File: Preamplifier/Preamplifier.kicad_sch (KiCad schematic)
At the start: 0 parts

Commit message: Preamplifier Schematic
Added the preamplifier schematic.
Updated the preamplifier project.
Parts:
- added C1, C10, C13, C14, C2, C23, C24, C5, C6, C9: 100n, Capacitor_SMD:C_0805_2012Metric_Pad1.18x1.45mm_HandSolder, symbol Device:C
- added C11, C12: 22n, Capacitor_SMD:C_0805_2012Metric_Pad1.18x1.45mm_HandSolder, symbol Device:C
- added C15, C16, C17, C18, C19, C20, C25, C26: 1u, Capacitor_SMD:C_0805_2012Metric_Pad1.18x1.45mm_HandSolder, symbol Device:C
- added C21, C22, C7, C8: 22u, Capacitor_SMD:CP_Elec_6.3x5.8, symbol Device:C_Polarized
- added C3, C4: 100p, Capacitor_SMD:C_0805_2012Metric_Pad1.18x1.45mm_HandSolder, symbol Device:C
- added H1, H2, H3, H4: MountingHole, MountingHole:MountingHole_3.2mm_M3, symbol Mechanical:MountingHole
- added J1: POWER, Connector_Molex:Molex_KK-254_AE-6410-03A_1x03_P2.54mm_Vertical, symbol Connector:Conn_01x03_Pin
- added J2: IN_L, Connector_Molex:Molex_KK-254_AE-6410-02A_1x02_P2.54mm_Vertical, symbol Connector_Generic:Conn_01x02
- added J3: IN_R, Connector_Molex:Molex_KK-254_AE-6410-02A_1x02_P2.54mm_Vertical, symbol Connector_Generic:Conn_01x02
- added J4: OUT_L, Connector_Molex:Molex_KK-254_AE-6410-02A_1x02_P2.54mm_Vertical, symbol Connector_Generic:Conn_01x02
- added J5: OUT_R, Connector_Molex:Molex_KK-254_AE-6410-02A_1x02_P2.54mm_Vertical, symbol Connector_Generic:Conn_01x02
- added R1, R11, R12, R2: 47K, Resistor_SMD:R_0805_2012Metric_Pad1.20x1.40mm_HandSolder, symbol Device:R
- added R10, R9: 10K, Resistor_SMD:R_0805_2012Metric_Pad1.20x1.40mm_HandSolder, symbol Device:R
- added R13, R14: 90K9, Resistor_SMD:R_0805_2012Metric_Pad1.20x1.40mm_HandSolder, symbol Device:R
- added R15, R16: 6K36, Resistor_SMD:R_0805_2012Metric_Pad1.20x1.40mm_HandSolder, symbol Device:R
- added R17, R18: 2K7, Resistor_SMD:R_0805_2012Metric_Pad1.20x1.40mm_HandSolder, symbol Device:R
- added R19, R20, R23, R24: 100K, Resistor_SMD:R_0805_2012Metric_Pad1.20x1.40mm_HandSolder, symbol Device:R
- added R21, R22: 750, Resistor_SMD:R_0805_2012Metric_Pad1.20x1.40mm_HandSolder, symbol Device:R
- added R3, R4: 2K2, Resistor_SMD:R_0805_2012Metric_Pad1.20x1.40mm_HandSolder, symbol Device:R
- added R5, R6: 4K7, Resistor_SMD:R_0805_2012Metric_Pad1.20x1.40mm_HandSolder, symbol Device:R
- added R7, R8: 180K, Resistor_SMD:R_0805_2012Metric_Pad1.20x1.40mm_HandSolder, symbol Device:R
- added U1, U2, U3, U4: OPA1612AxD, Package_SO:SOIC-8_3.9x4.9mm_P1.27mm, symbol Amplifier_Operational:OPA1612AxD
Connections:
- new net: C16.1, R10.2, R8.2, U3.1
- new net: C16.2, C18.1, R12.2
- new net: C2.1, U1.4 (V-)
- new net: C6.1, U2.4 (V-)
- new net: C5.2, U2.8 (V+)
- new net: C15.1, R7.2, R9.2, U1.1
- new net: C15.2, C17.1, R11.2
- new net: U1.6 (-), U1.7
- new net: C19.1, R11.1, U2.1, U2.2 (-)
- new net: C19.2, R15.1, U2.5 (+)
- new net: C26.2, J5.2 (Pin_2), R24.1
- new net: R17.1, R19.1, U2.6 (-)
- new net: R19.2, R21.1, U2.7
- new net: C25.2, J4.2 (Pin_2), R23.1
- new net: C23.1, C25.1, R21.2
- new net: C20.1, R12.1, U4.1, U4.2 (-)
- new net: C20.2, R16.1, U4.5 (+)
- new net: C4.1, J3.2 (Pin_2), R2.1, R4.1
- new net: R4.2, U3.3 (+)
- new net: C13.2, U4.8 (V+)
- new net: C3.1, J2.2 (Pin_2), R1.1, R3.1
- new net: C17.2, R13.1, U2.3 (+)
- new net: C11.1, R5.1, R7.1, U1.2 (-)
- new net: C7.1, R5.2
- new net: C1.2, U1.8 (V+)
- new net: C18.2, R14.1, U4.3 (+)
- new net: C14.1, U4.4 (V-)
- new net: R18.1, R20.1, U4.6 (-)
- new net: C22.1, R18.2
- new net: C12.1, R6.1, R8.1, U3.2 (-)
- new net: C12.2, R10.1
- new net: C24.1, C26.1, R22.2
- new net: C21.1, R17.2
- new net: C8.1, R6.2
- new net: C10.1, U3.4 (V-)
- new net: C9.2, U3.8 (V+)
- new net: R20.2, R22.1, U4.7
- new net: U3.6 (-), U3.7
- new net: C11.2, R9.1
- new net: R3.2, U1.3 (+)
- new net +12V: C1.1, C13.1, C5.1, C9.1, J1.1 (Pin_1)
- new net -12V: C10.2, C14.2, C2.2, C6.2, J1.3 (Pin_3)
- new net GND: C21.2, C22.2, C23.2, C24.2, C3.2, C4.2, C7.2, C8.2, J1.2 (Pin_2), J2.1 (Pin_1), J3.1 (Pin_1), J4.1 (Pin_1), J5.1 (Pin_1), R1.2, R13.2, R14.2, R15.2, R16.2, R2.2, R23.2, R24.2, U1.5 (+), U3.5 (+)

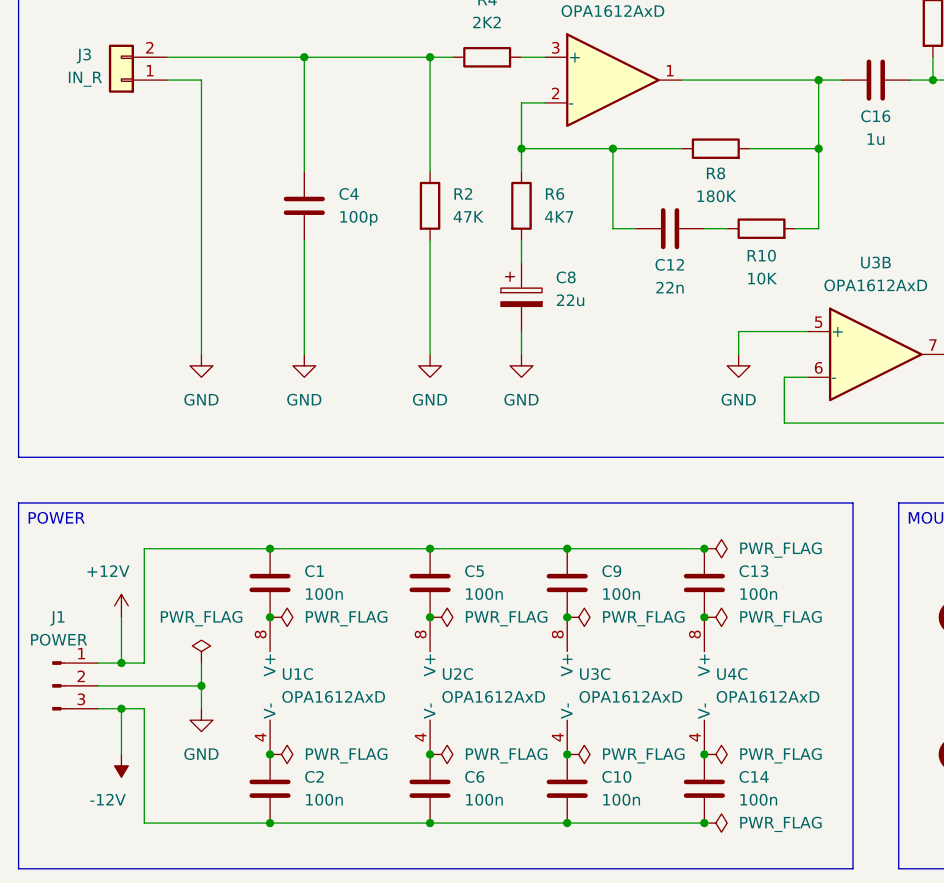
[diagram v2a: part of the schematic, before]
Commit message: Preamplifier Board
Updated the preamplifier board design.
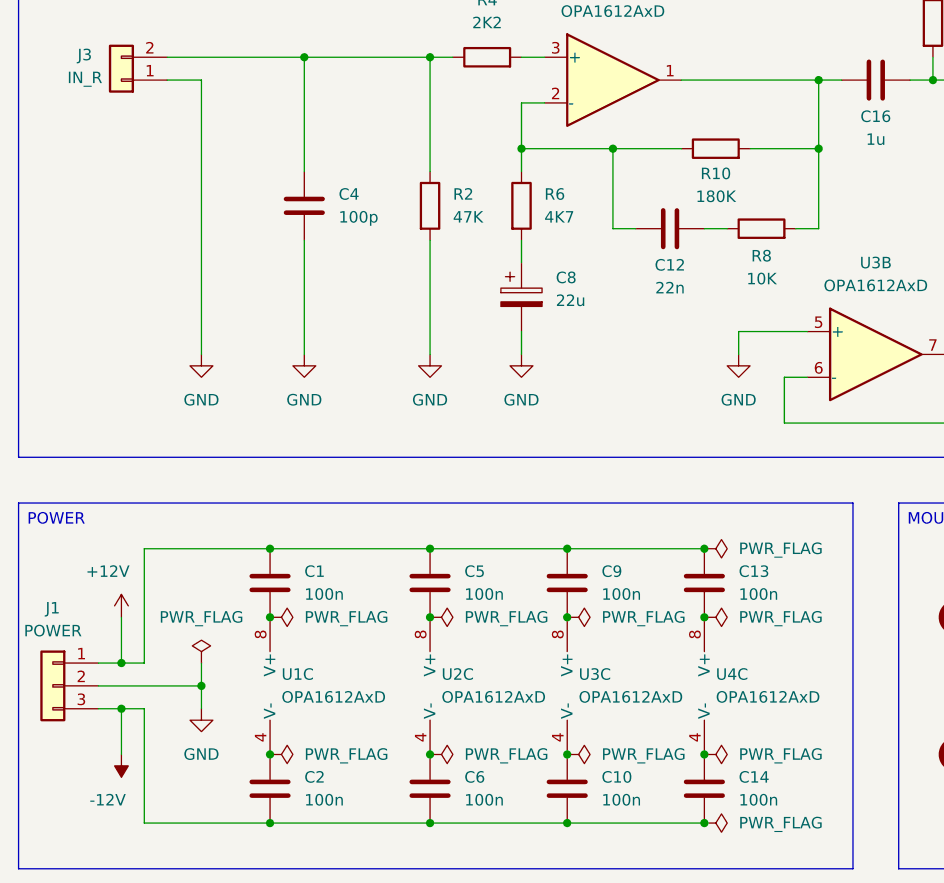
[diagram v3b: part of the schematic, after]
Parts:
- removed J1: POWER, Connector_Molex:Molex_KK-254_AE-6410-03A_1x03_P2.54mm_Vertical, symbol Connector:Conn_01x03_Pin
- added J1: POWER, Custom_Parts:Molex_KK-254_1x03_P2.54mm_Vertical, symbol Connector_Generic:Conn_01x03
- J2, J3, J4, J5: footprint Connector_Molex:Molex_KK-254_AE-6410-02A_1x02_P2.54mm_Vertical -> Custom_Parts:Molex_KK-254_1x02_P2.54mm_Vertical
- renumbered R8 to R10, R10 to R8
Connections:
- net +12V: now also J1.1 (Pin_1)
- net -12V: now also J1.3 (Pin_3)
- net GND: now also J1.2 (Pin_2)
- net at J5.2 (Pin_2), R24.1: now also C26.1; no longer C26.2
- net at C24.1, R22.2: now also C26.2; no longer C26.1
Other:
- moved on the sheet: C26
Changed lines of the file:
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@@
 			)
 		)
-		(property "Footprint" "Connector_Molex:Molex_KK-254_AE-6410-02A_1x02_P2.54mm_Vertical"
+		(property "Footprint" "Custom_Parts:Molex_KK-254_1x02_P2.54mm_Vertical"
 			(at 254 107.95 0)
 			(effects
@@
 	)
 	(symbol
-		(lib_id "Connector:Conn_01x03_Pin")
-		(at 30.48 172.72 0)
-		(unit 1)
-		(exclude_from_sim no)
-		(in_bom yes)
-		(on_board yes)
-		(dnp no)
-		(fields_autoplaced yes)
-		(property "Reference" "J1"
-			(at 31.115 165.1 0)
-			(effects
-				(font
-					(size 1.27 1.27)
-				)
-			)
-		)
-		(property "Value" "POWER"
-			(at 31.115 167.64 0)
-			(effects
-				(font
-					(size 1.27 1.27)
-				)
-			)
-		)
-		(property "Footprint" "Connector_Molex:Molex_KK-254_AE-6410-03A_1x03_P2.54mm_Vertical"
-			(at 30.48 172.72 0)
-			(effects
-				(font
-					(size 1.27 1.27)
-				)
-				(hide yes)
-			)
-		)
-		(property "Datasheet" "~"
-			(at 30.48 172.72 0)
-			(effects
-				(font
-					(size 1.27 1.27)
-				)
-				(hide yes)
-			)
-		)
-		(property "Description" "Generic connector, single row, 01x03, script generated"
-			(at 30.48 172.72 0)
-			(effects
-				(font
-					(size 1.27 1.27)
-				)
-				(hide yes)
-			)
-		)
-		(pin "1"
-		)
-		(pin "3"
-		)
-		(pin "2"
-		)
-		(instances
-			(project ""
-				(path "/506a4015-8700-461c-aa21-0f1930354b08"
-					(reference "J1")
-					(unit 1)
-				)
-			)
-		)
-	)
-	(symbol
 		(lib_id "power:GND")
 		(at 220.98 69.85 0)
@@
 		(dnp no)
 		(fields_autoplaced yes)
-		(property "Reference" "#FLG09"
+		(property "Reference" "#FLG010"
 			(at 104.775 180.34 0)
 			(effects
@@
 			(project "Preamplifier"
 				(path "/506a4015-8700-461c-aa21-0f1930354b08"
-					(reference "#FLG09")
+					(reference "#FLG010")
 					(unit 1)
 				)
@@
 			)
 		)
-		(property "Footprint" "Connector_Molex:Molex_KK-254_AE-6410-02A_1x02_P2.54mm_Vertical"
+		(property "Footprint" "Custom_Parts:Molex_KK-254_1x02_P2.54mm_Vertical"
 			(at 38.1 39.37 0)
 			(effects
@@
 			)
 		)
-		(property "Footprint" "Connector_Molex:Molex_KK-254_AE-6410-02A_1x02_P2.54mm_Vertical"
+		(property "Footprint" "Custom_Parts:Molex_KK-254_1x02_P2.54mm_Vertical"
 			(at 254 41.91 0)
 			(effects
@@
 	(symbol
 		(lib_id "Device:C")
-		(at 227.33 105.41 90)
+		(at 227.33 105.41 270)
+		(mirror x)
 		(unit 1)
 		(exclude_from_sim no)
@@
 		(on_board yes)
 		(dnp no)
-		(fields_autoplaced yes)
 		(property "Reference" "C26"
 			(at 227.33 97.79 90)
@@
 		)
 		(property "Footprint" "Capacitor_SMD:C_0805_2012Metric_Pad1.18x1.45mm_HandSolder"
-			(at 231.14 104.4448 0)
+			(at 223.52 104.4448 0)
 			(effects
 				(font
@@
 			)
 		)
-		(property "Footprint" "Connector_Molex:Molex_KK-254_AE-6410-02A_1x02_P2.54mm_Vertical"
+		(property "Footprint" "Custom_Parts:Molex_KK-254_1x02_P2.54mm_Vertical"
 			(at 38.1 105.41 0)
 			(effects
@@
 		(on_board yes)
 		(dnp no)
-		(property "Reference" "R10"
+		(property "Reference" "R8"
 			(at 109.22 124.968 90)
 			(effects
@@
 			(project "Preamplifier"
 				(path "/506a4015-8700-461c-aa21-0f1930354b08"
-					(reference "R10")
+					(reference "R8")
 					(unit 1)
 				)
@@
 		(dnp no)
 		(fields_autoplaced yes)
-		(property "Reference" "#FLG08"
+		(property "Reference" "#FLG09"
 			(at 104.775 165.1 0)
 			(effects
@@
 			(project "Preamplifier"
 				(path "/506a4015-8700-461c-aa21-0f1930354b08"
-					(reference "#FLG08")
+					(reference "#FLG09")
 					(unit 1)
 				)
@@
 		(on_board yes)
 		(dnp no)
-		(property "Reference" "R8"
+		(property "Reference" "R10"
 			(at 104.14 115.824 90)
 			(effects
@@
 			(project "Preamplifier"
 				(path "/506a4015-8700-461c-aa21-0f1930354b08"
-					(reference "R8")
+					(reference "R10")
 					(unit 1)
 				)
@@
 	)
 	(symbol
+		(lib_id "Connector_Generic:Conn_01x03")
+		(at 30.48 172.72 0)
+		(mirror y)
+		(unit 1)
+		(exclude_from_sim no)
+		(in_bom yes)
+		(on_board yes)
+		(dnp no)
+		(property "Reference" "J1"
+			(at 30.48 164.084 0)
+			(effects
+				(font
+					(size 1.27 1.27)
+				)
+			)
+		)
+		(property "Value" "POWER"
+			(at 30.48 166.624 0)
+			(effects
+				(font
+					(size 1.27 1.27)
+				)
+			)
+		)
+		(property "Footprint" "Custom_Parts:Molex_KK-254_1x03_P2.54mm_Vertical"
+			(at 30.48 172.72 0)
+			(effects
+				(font
+					(size 1.27 1.27)
+				)
+				(hide yes)
+			)
+		)
+		(property "Datasheet" "~"
+			(at 30.48 172.72 0)
+			(effects
+				(font
+					(size 1.27 1.27)
+				)
+				(hide yes)
+			)
+		)
+		(property "Description" "Generic connector, single row, 01x03, script generated (kicad-library-utils/schlib/autogen/connector/)"
+			(at 30.48 172.72 0)
+			(effects
+				(font
+					(size 1.27 1.27)
+				)
+				(hide yes)
+			)
+		)
+		(pin "1"
+		)
+		(pin "2"
+		)
+		(pin "3"
+		)
+		(instances
+			(project ""
+				(path "/506a4015-8700-461c-aa21-0f1930354b08"
+					(reference "J1")
+					(unit 1)
+				)
+			)
+		)
+	)
+	(symbol
 		(lib_id "Device:R")
 		(at 185.42 53.34 0)
@@
 		(dnp no)
 		(fields_autoplaced yes)
-		(property "Reference" "#FLG010"
+		(property "Reference" "#FLG08"
 			(at 104.775 157.48 0)
 			(effects
@@
 			(project "Preamplifier"
 				(path "/506a4015-8700-461c-aa21-0f1930354b08"
-					(reference "#FLG010")
+					(reference "#FLG08")
 					(unit 1)
 				)

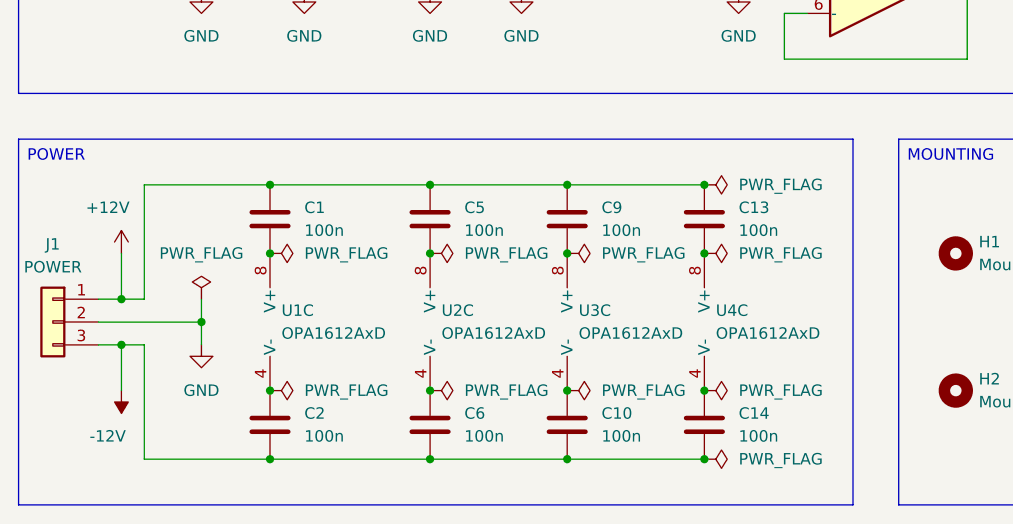
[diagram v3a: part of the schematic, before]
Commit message: Preamplifier Board
Updated the preamplifier schematic.
Updated the preamplifier board design.
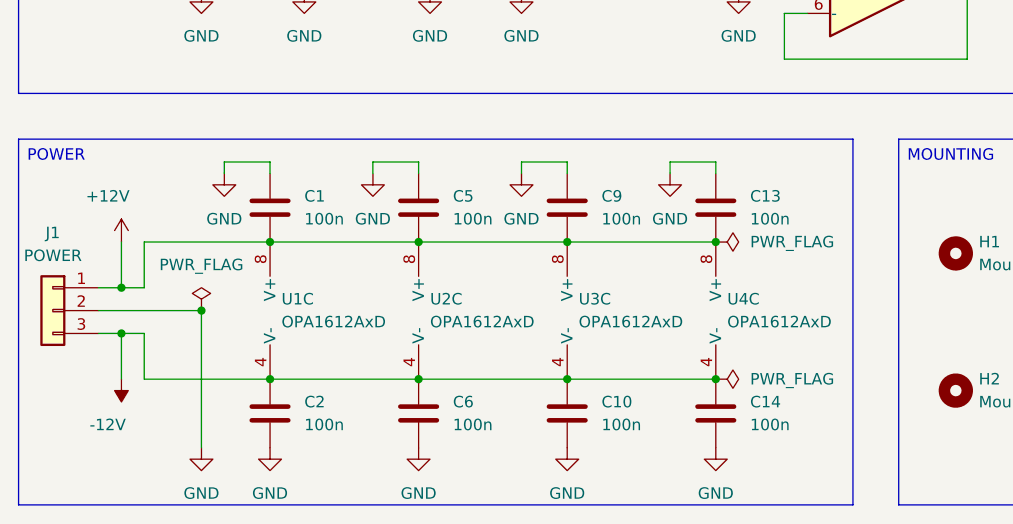
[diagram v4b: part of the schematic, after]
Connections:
- net +12V: now also C1.2, C13.2, C5.2, C9.2, U1.8 (V+), U2.8 (V+), U3.8 (V+), U4.8 (V+); no longer C1.1, C13.1, C5.1, C9.1
- net -12V: now also C10.1, C14.1, C2.1, C6.1, U1.4 (V-), U2.4 (V-), U3.4 (V-), U4.4 (V-); no longer C10.2, C14.2, C2.2, C6.2
- net GND: now also C1.1, C10.2, C13.1, C14.2, C2.2, C5.1, C6.2, C9.1
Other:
- moved on the sheet: C1, C10, C13, C14, C2, C5, C6, C9, J1, U1C, U2C, U3C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

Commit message: Company name
Updated the company name for all project files.
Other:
- company: Chapuzas S.L. -> DavidMolTor
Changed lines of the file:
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@@
 		(date "2025-08-08")
 		(rev "1.0")
-		(company "Chapuzas S.L.")
+		(company "DavidMolTor")
 	)
 	(text_box "LEFT CHANNEL"
